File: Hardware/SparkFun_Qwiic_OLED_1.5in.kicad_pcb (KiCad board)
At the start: 2 copper layers, 34.3 x 48.3 mm, 61 parts, among them J1 Qwiic_RA, J2 Qwiic_RA, J3 Conn_01x06, J4 Conn_01x24_FPC, U2 WEO128128ASAP3N00000, U5 AP3012

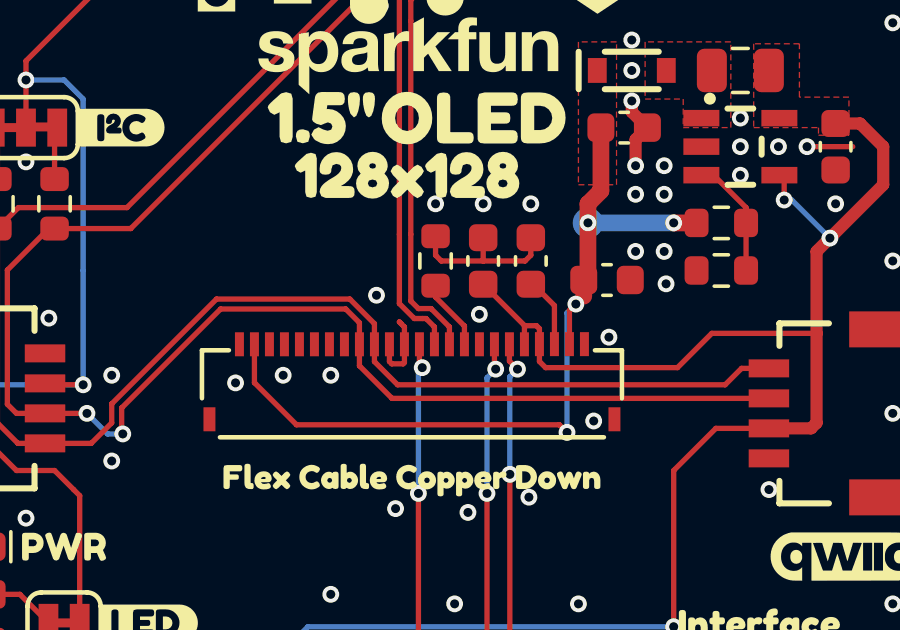
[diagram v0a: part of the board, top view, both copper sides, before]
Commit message: Adds no-connect on pin 5, adds prod-id value for 569k resistor
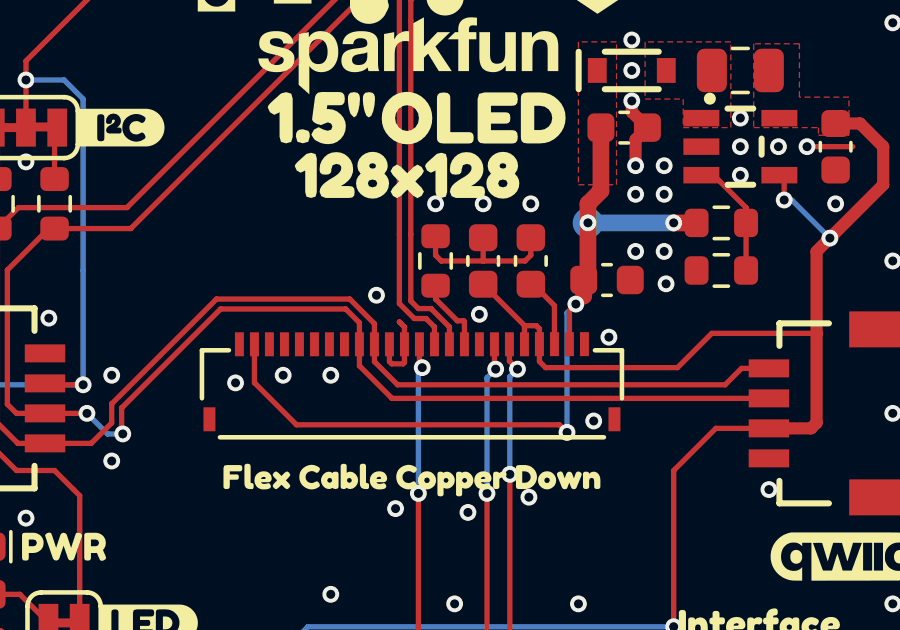
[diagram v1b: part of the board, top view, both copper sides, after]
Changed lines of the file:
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@@
 			(psa4output no)
 			(plot_black_and_white yes)
-			(plotinvisibletext no)
 			(sketchpadsonfab no)
 			(plotpadnumbers no)
@@
 	(segment
 		(start 142.326 84.3735)
-		(end 142.326 83.765)
+		(end 142.326 83.614644)
 		(width 0.1778)
 		(layer "F.Cu")
@@
 	)
 	(segment
-		(start 142.326 83.765)
-		(end 141.3635 82.8025)
+		(start 141.3635 82.864812)
+		(end 141.3635 82.421)
 		(width 0.1778)
 		(layer "F.Cu")
@@
 	)
 	(segment
-		(start 141.3635 82.8025)
-		(end 141.3635 82.421)
+		(start 142.089032 83.590344)
+		(end 141.3635 82.864812)
+		(width 0.1778)
+		(layer "F.Cu")
+		(net 22)
+	)
+	(segment
+		(start 142.3017 83.590344)
+		(end 142.089032 83.590344)
+		(width 0.1778)
+		(layer "F.Cu")
+		(net 22)
+	)
+	(segment
+		(start 142.326 83.614644)
+		(end 142.3017 83.590344)
 		(width 0.1778)
 		(layer "F.Cu")

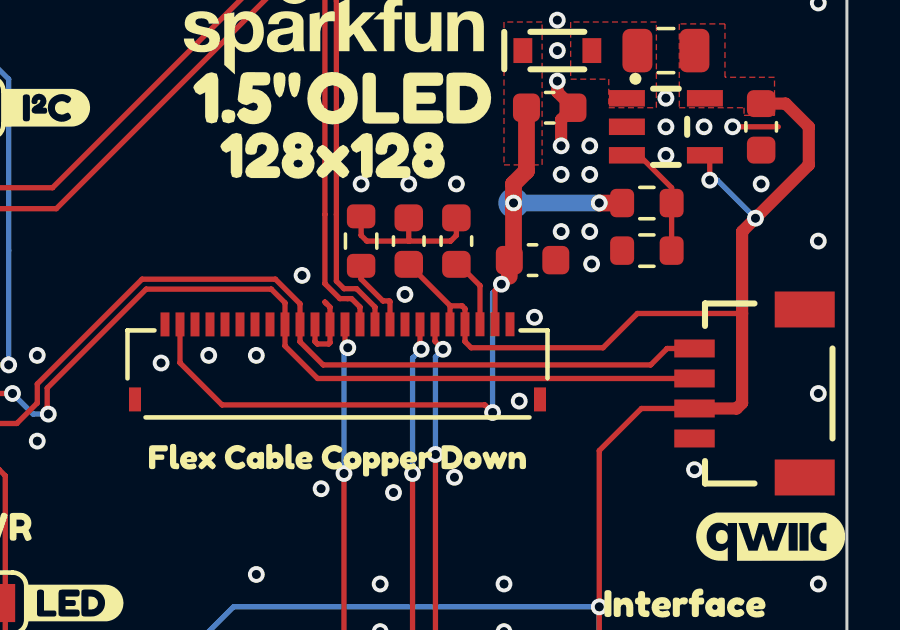
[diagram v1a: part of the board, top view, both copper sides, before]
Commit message: Updates PCB with aforementioned changes
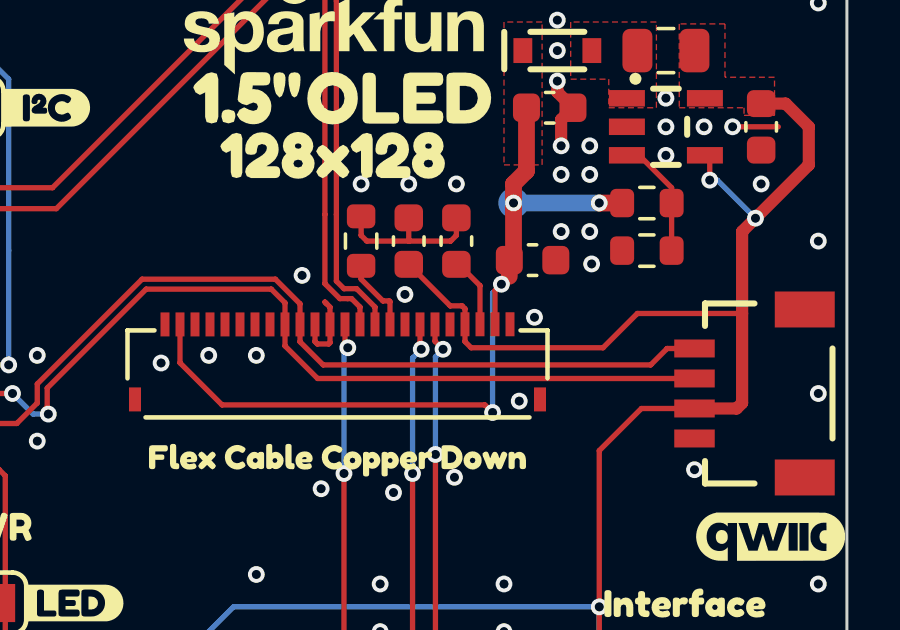
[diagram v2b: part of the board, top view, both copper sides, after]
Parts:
- JP2: value ~ -> I2C
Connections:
- J4 pad 20: 3.3V -> unconnected-(J4-Pin_20-Pad20)
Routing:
- net 3.3V: track 115.8 -> 115.2 mm
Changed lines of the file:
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@@
 	(net 23 "Net-(J4-Pin_18)")
 	(net 24 "/12V_OUT")
+	(net 25 "unconnected-(J4-Pin_20-Pad20)")
 	(footprint "SparkFun-Resistor:R_0603_1608Metric"
 		(layer "F.Cu")
@@
 			)
 		)
-		(property "PROD_ID" "RES-..."
+		(property "PROD_ID" "RES-26754"
 			(at 0 0 270)
 			(unlocked yes)
@@
 			)
 		)
-		(property "Value" "~"
+		(property "Value" "I2C"
 			(at 0 1.143 0)
 			(layer "F.Fab")
@@
 			(size 0.3 0.8)
 			(layers "F.Cu" "F.Mask" "F.Paste")
-			(net 1 "3.3V")
+			(net 25 "unconnected-(J4-Pin_20-Pad20)")
 			(pinfunction "Pin_20")
-			(pintype "passive")
+			(pintype "passive+no_connect")
 			(solder_paste_margin_ratio -0.1)
 			(thermal_bridge_angle 0)
@@
 		(width 0.1778)
 		(layer "F.Cu")
-		(net 1)
-	)
-	(segment
-		(start 144.326 84.3735)
-		(end 144.326 83.746)
-		(width 0.1778)
-		(layer "F.Cu")

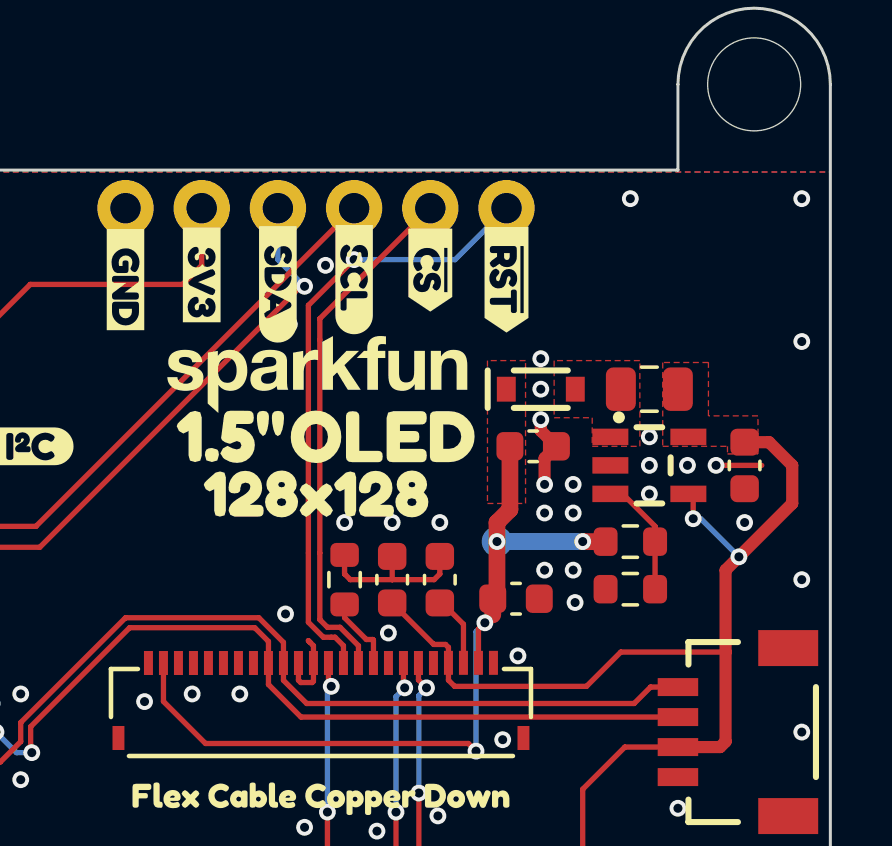
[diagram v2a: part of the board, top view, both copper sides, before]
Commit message: Adds D/C to PTH header for SPI funcitonality
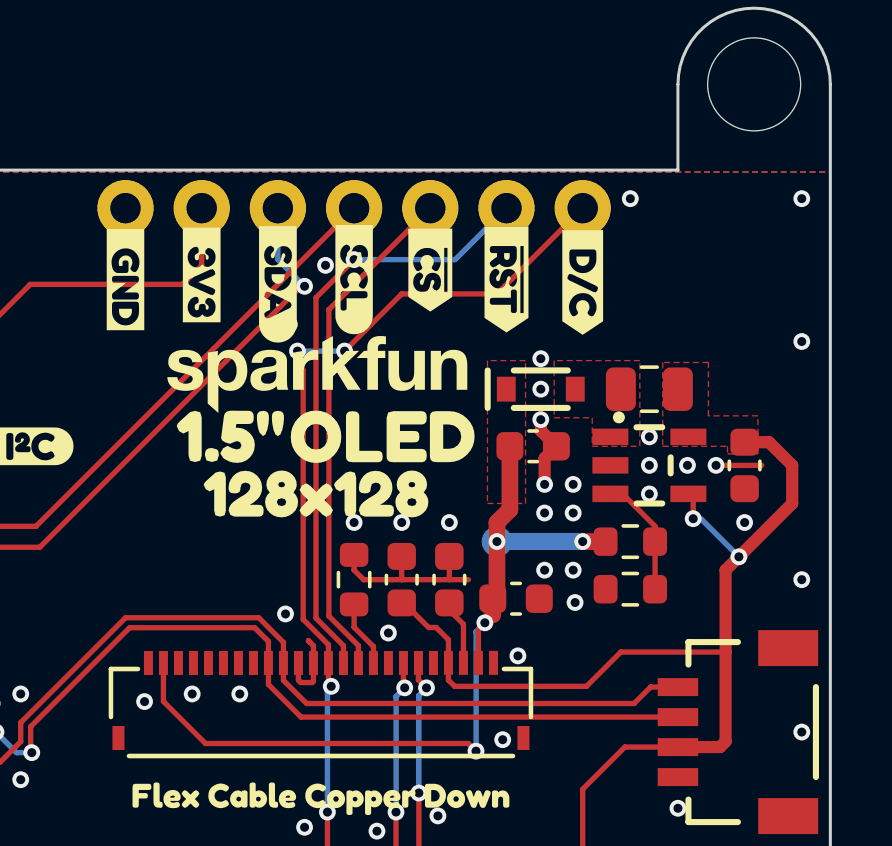
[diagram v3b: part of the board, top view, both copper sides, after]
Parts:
- removed J3: Conn_01x06, SparkFun-Connector:1x06
- added J5: Conn_01x07, SparkFun-Connector:1x07, F.Cu at (134.1, 69.2)
- added kibuzzard-685B1775: G***, kibuzzard-685B1775, F.Cu at (149.3, 71.7)
- moved R6 0.32 mm to (141.7, 81.6)
- moved C3 0.32 mm to (144.9, 81.6)
- moved C4 0.32 mm to (143.3, 81.6)
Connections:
- net Net-(J4-Pin_13) renamed D/C
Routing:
- net D/C: track 31.5 -> 53.8 mm, vias 2 -> 4
- net GND: track 12.3 -> 13.0 mm

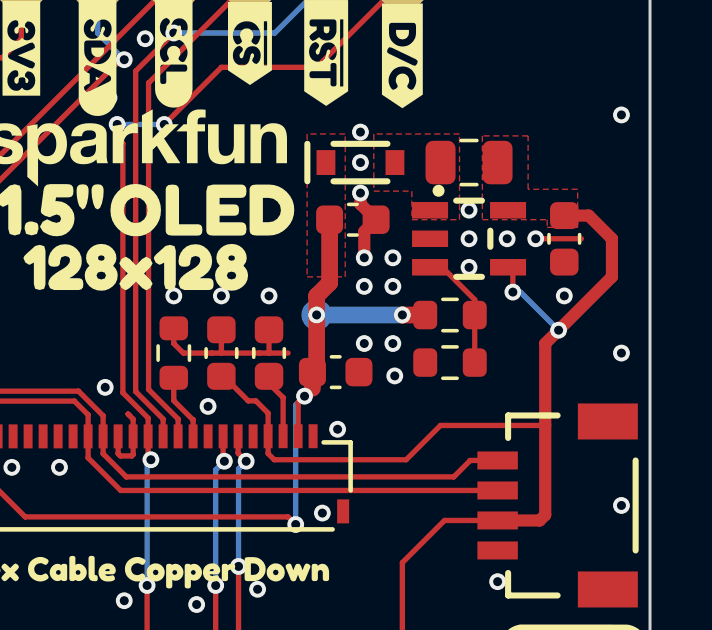
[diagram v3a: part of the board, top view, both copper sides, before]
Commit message: Changes certain resistors to use more common values
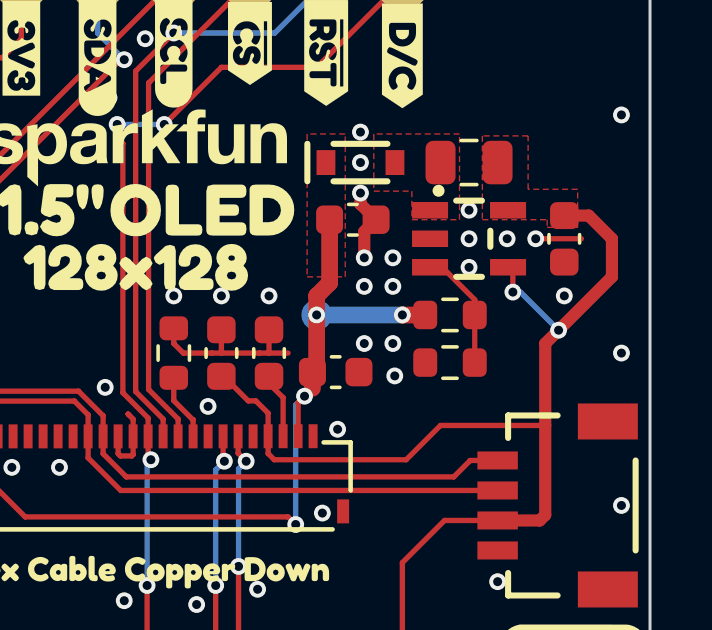
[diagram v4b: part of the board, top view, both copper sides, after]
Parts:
- removed R12: 68.1k, SparkFun-Resistor:R_0603_1608Metric
- removed R9: 7.5k, SparkFun-Resistor:R_0603_1608Metric
- added R1: 18k, SparkFun-Resistor:R_0603_1608Metric, F.Cu at (150.9, 80.3)
- added R2: 2.1k, SparkFun-Resistor:R_0603_1608Metric, F.Cu at (150.9, 81.9)
- R6: value 569k -> 536k

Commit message: Updates to v10
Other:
- board text added: "v10"
- board text removed: "v01"
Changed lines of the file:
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@@
 	(title_block
 		(title "SparkFun 1.5\" OLED")
-		(date "2025-04-11")
-		(rev "v01")
+		(date "2025-08-06")
+		(rev "v10")
 		(company "SparkFun Electronics")
 		(comment 1 "Designed By: N. Seidle")
@@
 		(layer "Edge.Cuts")
 	)
-	(gr_text "v01"
+	(gr_text "v10"
 		(at 128.6635 104.1385 0)
 		(layer "F.Cu" knockout)
@@
 			(keep_text_aligned yes)
 		)
-		(gr_text "0.85 in"
+		(gr_text "21.59 mm"
 			(at 158.946 97.471 90)
 			(layer "Dwgs.User")
@@
 			(keep_text_aligned yes)
 		)
-		(gr_text "1.475 in"
+		(gr_text "37.465 mm"
 			(at 168.471 86.676 90)
 			(layer "Dwgs.User")
@@
 			(extension_offset 0.5)
 		)
-		(gr_text "1.35 in"
+		(gr_text "34.29 mm"
 			(at 140.411 56.9855 0)
 			(layer "Dwgs.User")
@@
 			(keep_text_aligned yes)
 		)
-		(gr_text "0.21 in"
+		(gr_text "5.4 mm"
 			(at 130.5685 105.726 90)
 			(layer "Dwgs.User")
@@
 			(keep_text_aligned yes)
 		)
-		(gr_text "1.15 in"
+		(gr_text "29.21 mm"
 			(at 140.411 110.926 0)
 			(layer "Dwgs.User")
@@
 			(extension_offset 0.5)
 		)
-		(gr_text "0.1 in"
+		(gr_text "2.54 mm"
 			(at 124.536 59.8085 0)
 			(layer "Dwgs.User")
@@
 			(keep_text_aligned yes)
 		)
-		(gr_text "1.7 in"
+		(gr_text "43.18 mm"
 			(at 162.4385 86.676 90)
 			(layer "Dwgs.User")
@@
 			(extension_offset 0.5)
 		)
-		(gr_text "1.9 in"
+		(gr_text "48.26 mm"
 			(at 120.211 86.676 90)
 			(layer "Dwgs.User")

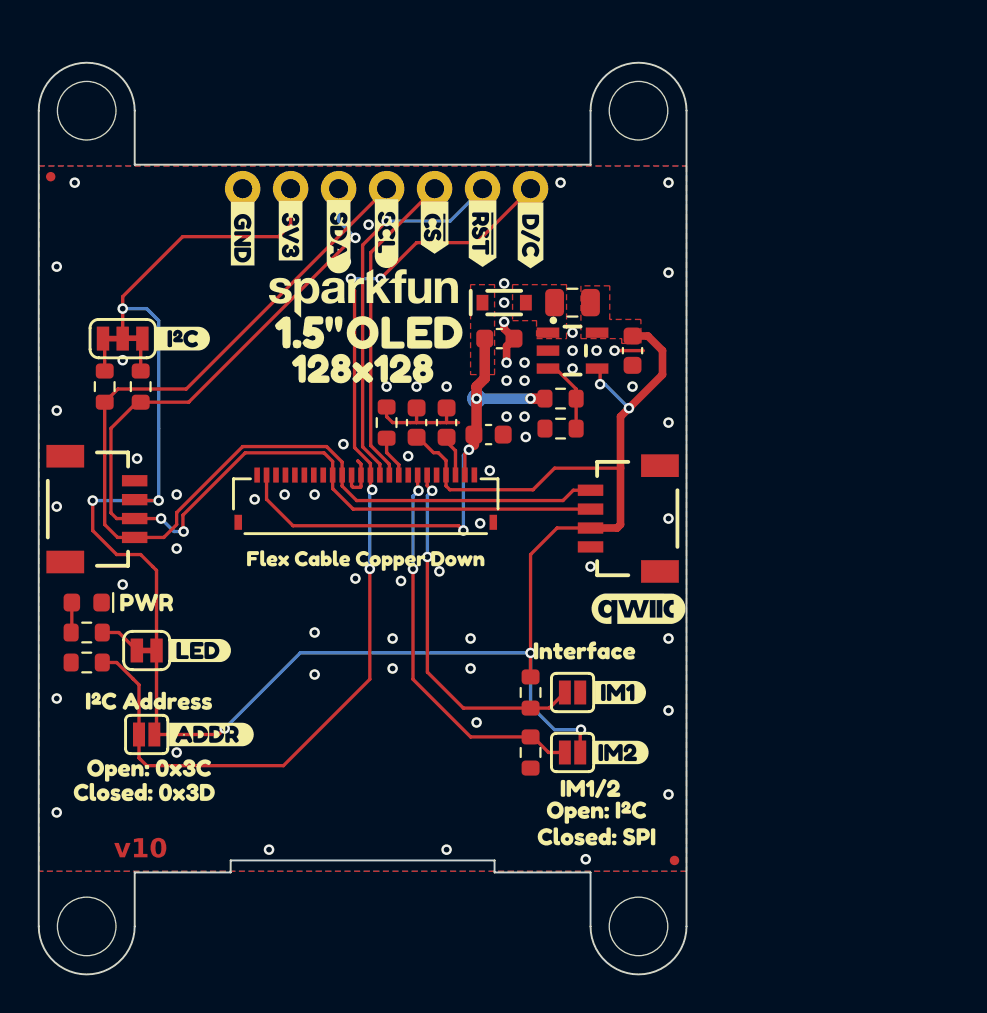
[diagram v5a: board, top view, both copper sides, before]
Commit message: Cleans up schematic, adds table to silk for interface settings
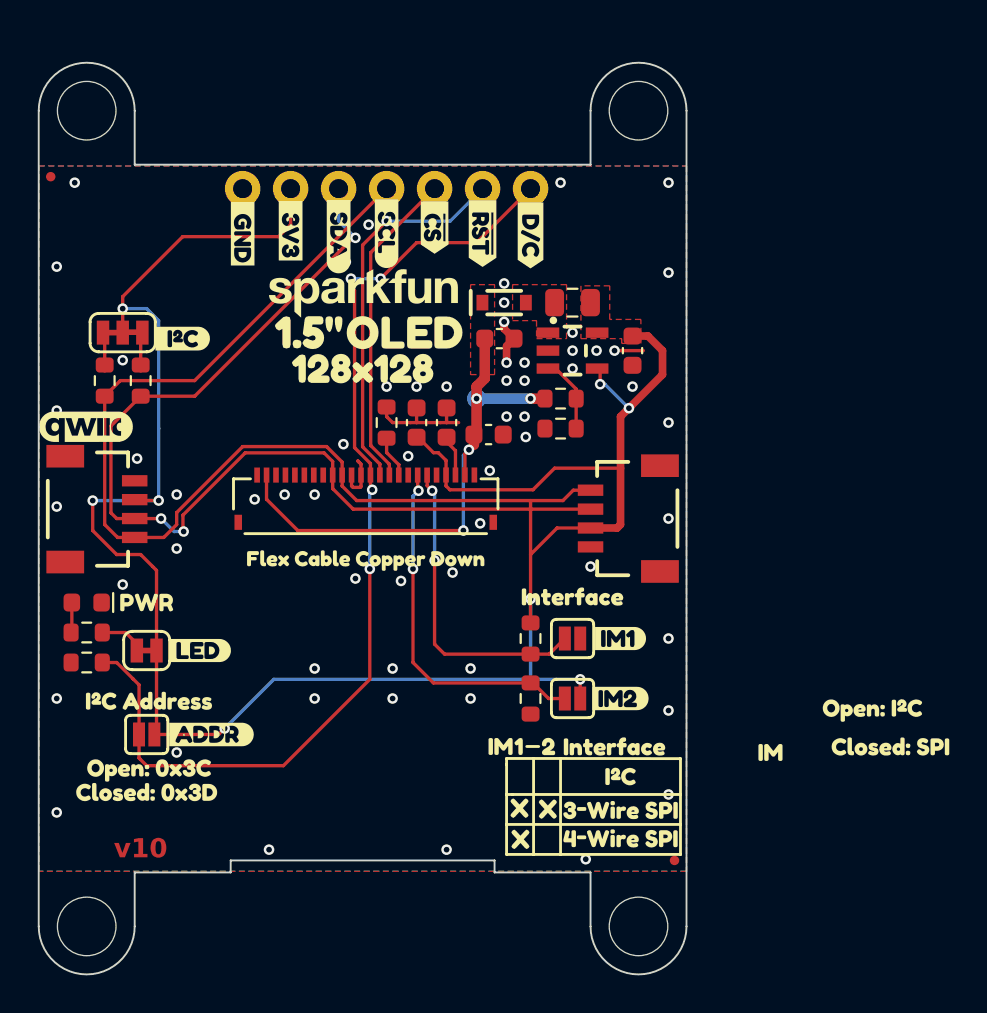
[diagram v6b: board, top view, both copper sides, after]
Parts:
- removed kibuzzard-680FC9DC: G***, kibuzzard-680FC9DC
- added kibuzzard-689381EF: G***, kibuzzard-689381EF, F.Cu at (150.2, 102.1)
- added kibuzzard-689381EF: G***, kibuzzard-689381EF, F.Cu at (148.8, 103.7)
- added kibuzzard-689381EF: G***, kibuzzard-689381EF, F.Cu at (148.7, 102.0)
- added kibuzzard-68938227: G***, kibuzzard-68938227, F.Cu at (162.0, 99.1)
- added kibuzzard-6893822D: G***, kibuzzard-6893822D, F.Cu at (147.7, 98.7)
- added kibuzzard-68938236: G***, kibuzzard-68938236, F.Cu at (148.7, 98.7)
- added kibuzzard-68938244: G***, kibuzzard-68938244, F.Cu at (153.7, 98.7)
- added kibuzzard-6893824B: G***, kibuzzard-6893824B, F.Cu at (150.3, 98.7)
- added kibuzzard-68938257: G***, kibuzzard-68938257, F.Cu at (154.1, 100.3)
- added kibuzzard-68938266: G***, kibuzzard-68938266, F.Cu at (154.1, 102.1)
- added kibuzzard-68938270: G***, kibuzzard-68938270, F.Cu at (154.1, 103.6)
- moved G*** 30.8 mm to (125.8, 81.8)
- moved kibuzzard-680FCA02 16.3 mm to (168.4, 98.7)
- moved kibuzzard-680FCAD6 15.6 mm to (167.4, 96.8)
- moved kibuzzard-680FCAEB 2.93 mm to (151.5, 90.8)
- moved JP6 2.86 mm to (151.5, 93.0)
- moved JP7 2.86 mm to (151.5, 96.2)
- moved R10 2.86 mm to (149.3, 93.0)
- moved R11 2.86 mm to (149.3, 96.2)
- moved kibuzzard-680FC897 2.86 mm to (154.1, 96.2)
- moved kibuzzard-680FC89E 2.86 mm to (154.1, 93.0)
- moved JP2 0.32 mm to (127.7, 76.8)
- moved R4 0.32 mm to (128.7, 79.4)
- moved R5 0.32 mm to (126.8, 79.4)
- moved kibuzzard-680FCA9D 0.13 mm to (129.0, 101.2)
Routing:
- net Net-(J4-Pin_19): track 19.1 -> 16.6 mm
- net Net-(J4-Pin_18): track 20.6 -> 18.9 mm
- net GND: vias 62 -> 61
